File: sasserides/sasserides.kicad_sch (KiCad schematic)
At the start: 129 parts, among them J1 Conn_02x16_Odd_Even, Q1 2N7002

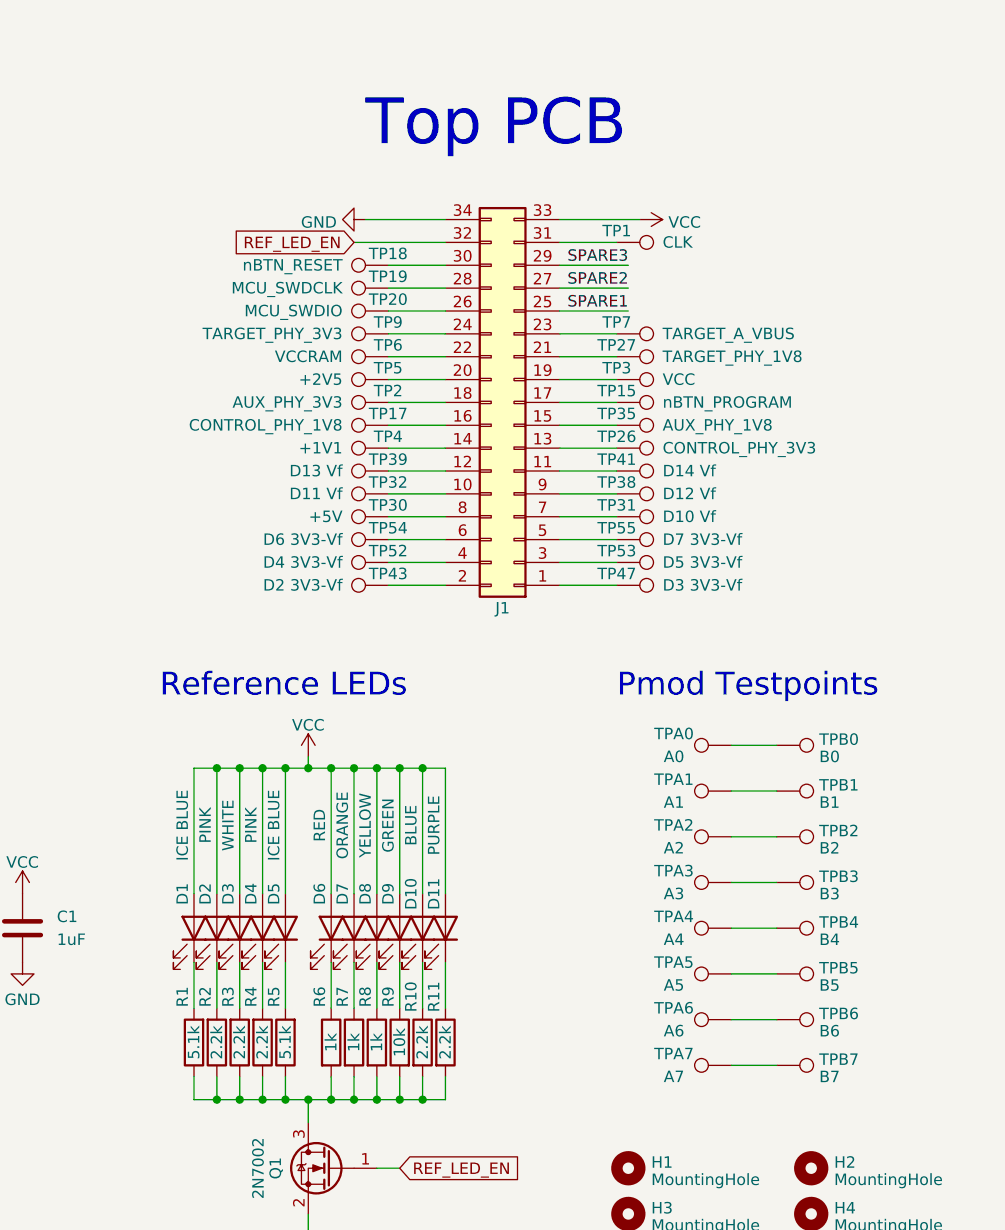
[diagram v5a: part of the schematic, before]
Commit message: Give all nets meaningful names.
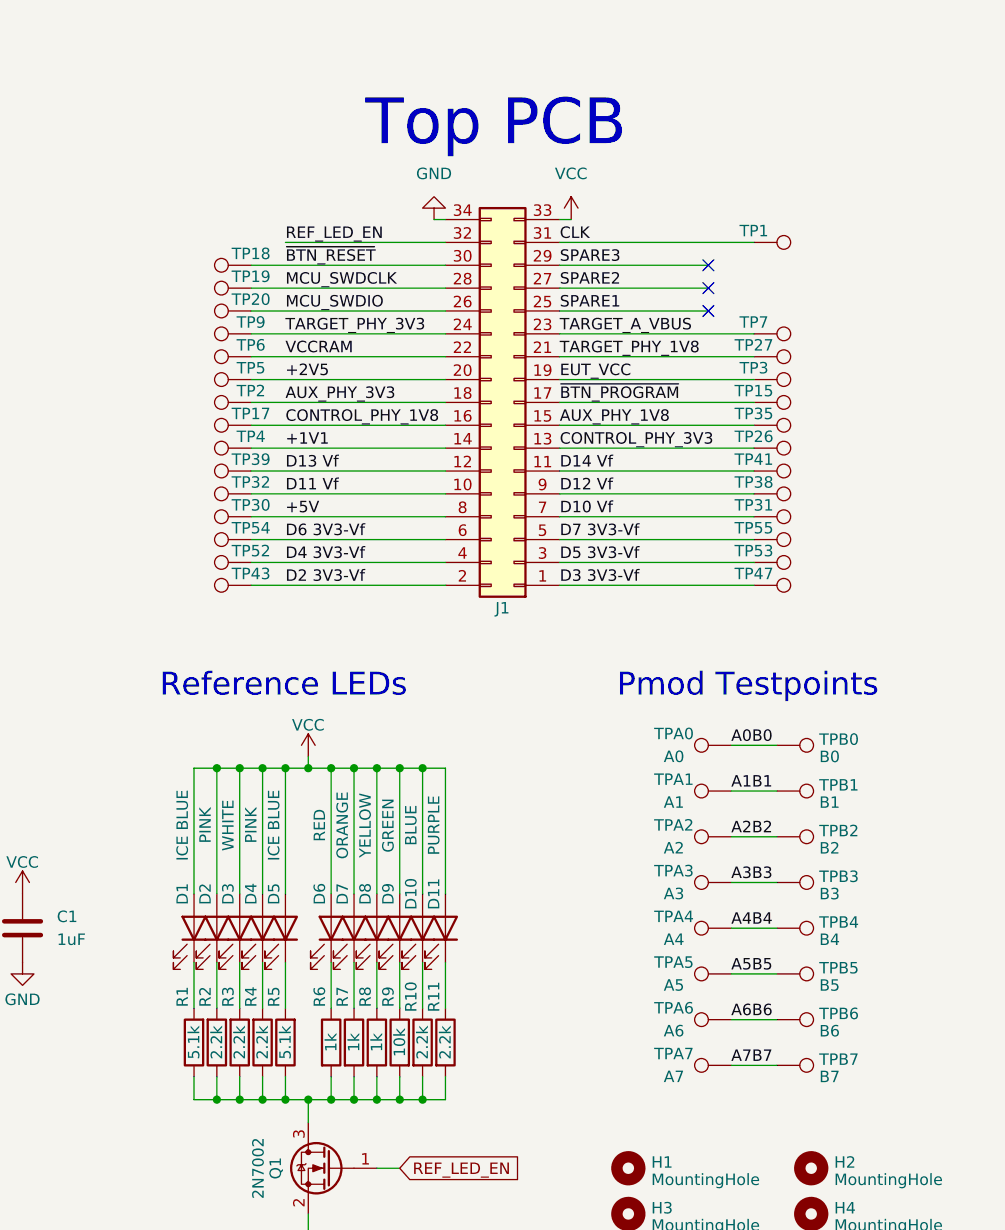
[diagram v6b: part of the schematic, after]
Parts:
- TP1: value CLK -> ~
- TP15: value nBTN_PROGRAM -> ~
- TP17: value CONTROL_PHY_1V8 -> ~
- TP18: value nBTN_RESET -> ~
- TP19: value MCU_SWDCLK -> ~
- TP2: value AUX_PHY_3V3 -> ~
- TP20: value MCU_SWDIO -> ~
- TP26: value CONTROL_PHY_3V3 -> ~
- TP27: value TARGET_PHY_1V8 -> ~
- TP3: value VCC -> ~
- TP30: value +5V -> ~
- TP31: value D10 Vf -> ~
- TP32: value D11 Vf -> ~
- TP35: value AUX_PHY_1V8 -> ~
- TP38: value D12 Vf -> ~
- TP39: value D13 Vf -> ~
- TP4: value +1V1 -> ~
- TP41: value D14 Vf -> ~
- TP43: value D2 3V3-Vf -> ~
- TP47: value D3 3V3-Vf -> ~
- TP5: value +2V5 -> ~
- TP52: value D4 3V3-Vf -> ~
- TP53: value D5 3V3-Vf -> ~
- TP54: value D6 3V3-Vf -> ~
- TP55: value D7 3V3-Vf -> ~
- TP6: value VCCRAM -> ~
- TP7: value TARGET_A_VBUS -> ~
- TP9: value TARGET_PHY_3V3 -> ~
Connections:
- net D3 3V3-Vf: now reaches J1.1 (Pin_1), TP47.1
- net A0B0: now reaches TPA0.1, TPB0.1
- net D11 Vf: now reaches J1.10 (Pin_10), TP32.1
- net D14 Vf: now reaches J1.11 (Pin_11), TP41.1
- net D13 Vf: now reaches J1.12 (Pin_12), TP39.1
- net CONTROL_PHY_3V3: now reaches J1.13 (Pin_13), TP26.1
- net +1V1: now reaches J1.14 (Pin_14), TP4.1
- net AUX_PHY_1V8: now reaches J1.15 (Pin_15), TP35.1
- net CONTROL_PHY_1V8: now reaches J1.16 (Pin_16), TP17.1
- net ~{BTN_PROGRAM}: now reaches J1.17 (Pin_17), TP15.1
- net AUX_PHY_3V3: now reaches J1.18 (Pin_18), TP2.1
- net EUT_VCC: now reaches J1.19 (Pin_19), TP3.1
- net D2 3V3-Vf: now reaches J1.2 (Pin_2), TP43.1
- net +2V5: now reaches J1.20 (Pin_20), TP5.1
- net TARGET_PHY_1V8: now reaches J1.21 (Pin_21), TP27.1
- net VCCRAM: now reaches J1.22 (Pin_22), TP6.1
- net TARGET_A_VBUS: now reaches J1.23 (Pin_23), TP7.1
- net TARGET_PHY_3V3: now reaches J1.24 (Pin_24), TP9.1
- net MCU_SWDIO: now reaches J1.26 (Pin_26), TP20.1
- net MCU_SWDCLK: now reaches J1.28 (Pin_28), TP19.1
- net D5 3V3-Vf: now reaches J1.3 (Pin_3), TP53.1
- net ~{BTN_RESET}: now reaches J1.30 (Pin_30), TP18.1
- net CLK: now reaches J1.31 (Pin_31), TP1.1
- net D4 3V3-Vf: now reaches J1.4 (Pin_4), TP52.1
- net D7 3V3-Vf: now reaches J1.5 (Pin_5), TP55.1
- net D6 3V3-Vf: now reaches J1.6 (Pin_6), TP54.1
- net D10 Vf: now reaches J1.7 (Pin_7), TP31.1
- net +5V: now reaches J1.8 (Pin_8), TP30.1
- net D12 Vf: now reaches J1.9 (Pin_9), TP38.1
- net A3B3: now reaches TPA3.1, TPB3.1
- net A2B2: now reaches TPA2.1, TPB2.1
- net A1B1: now reaches TPA1.1, TPB1.1
- net A5B5: now reaches TPA5.1, TPB5.1
- net A6B6: now reaches TPA6.1, TPB6.1
- net A4B4: now reaches TPA4.1, TPB4.1
- net A7B7: now reaches TPA7.1, TPB7.1
- no-connect marks 44 -> 47
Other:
- moved on the sheet: TP1, TP15, TP17, TP18, TP19, TP2, TP20, TP26, TP27, TP3, TP30, TP31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

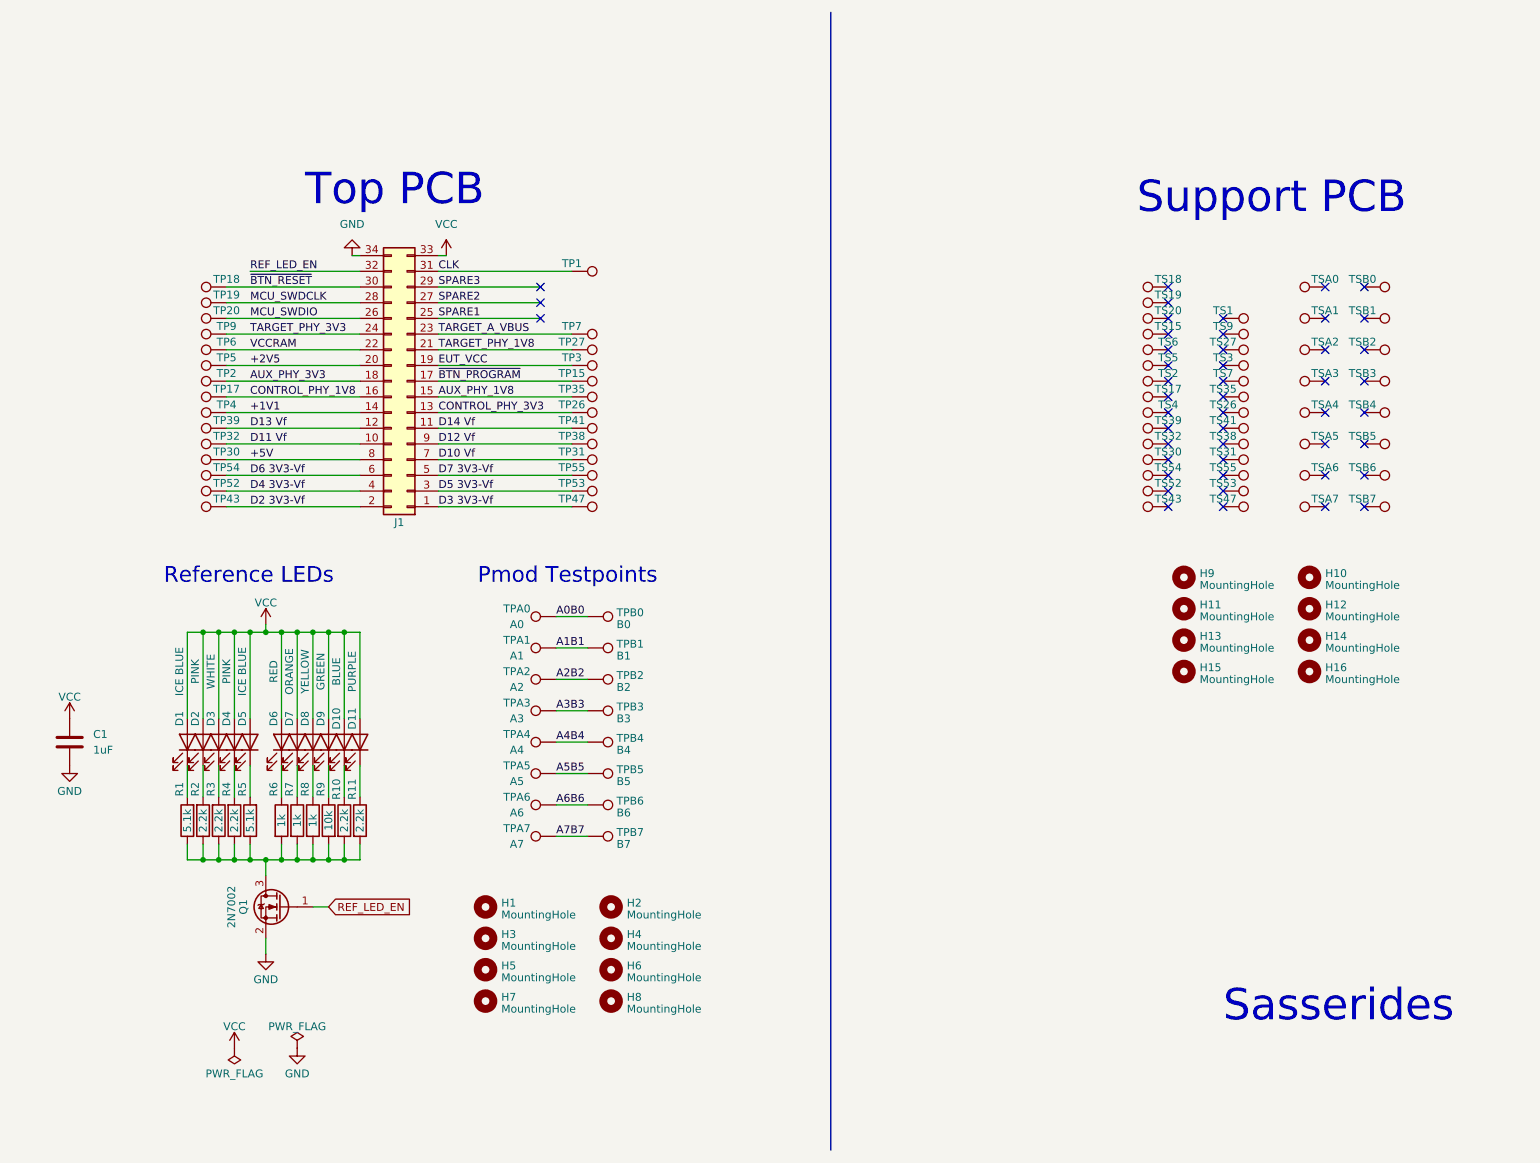
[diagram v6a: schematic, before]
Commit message: Add clock buffer and revise layout.
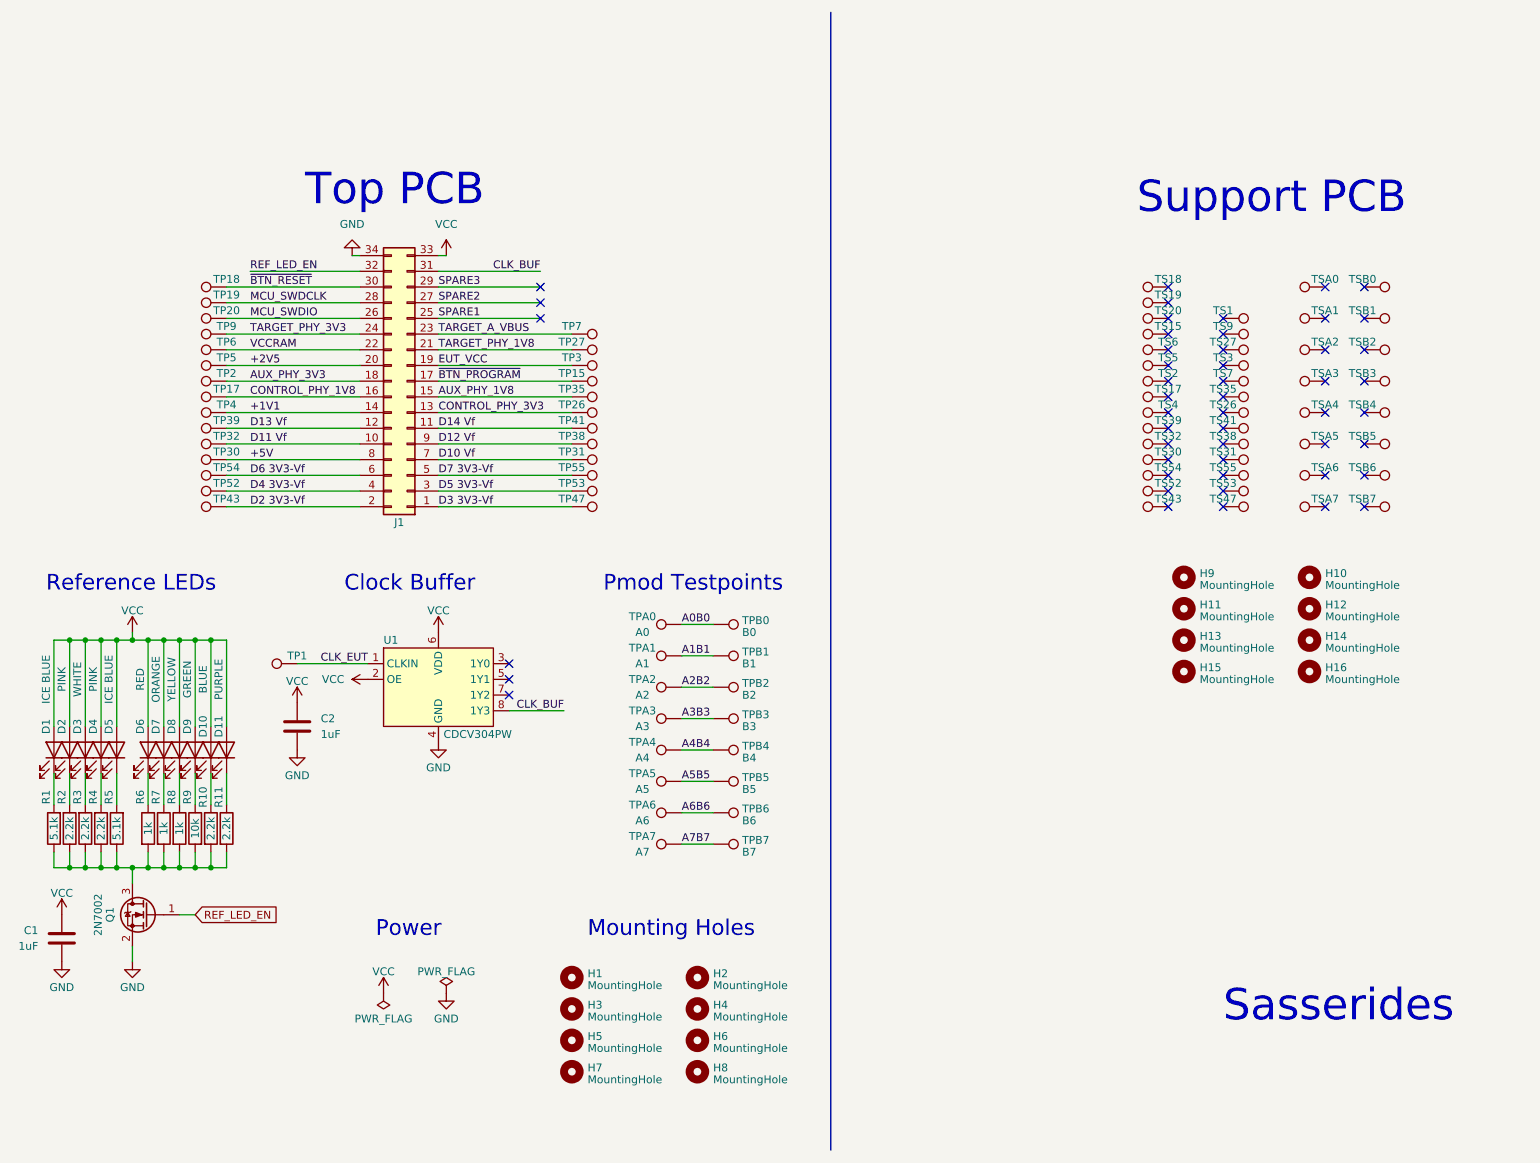
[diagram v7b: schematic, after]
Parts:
- added C2: 1uF, Capacitor_SMD:C_0805_2012Metric, symbol Device:C
- added U1: CDCV304PW, Package_SO:TSSOP-8_4.4x3mm_P0.65mm, symbol tycho:CDCV304PW
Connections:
- net GND: now also C2.2, U1.4 (GND)
- net VCC: now also C2.1, U1.2 (OE), U1.6 (VDD)
- net CLK renamed CLK_BUF
- net CLK_BUF: now also U1.8 (1Y3); no longer TP1.1
- new net CLK_EUT: TP1.1, U1.1 (CLKIN)
- no-connect marks 47 -> 50
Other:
- note added: "Clock Buffer"
- note added: "Mounting Holes"
- note added: "Power"
- moved on the sheet: C1, D1, D10, D11, D2, D3, D4, D5, D6, D7, D8, D9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

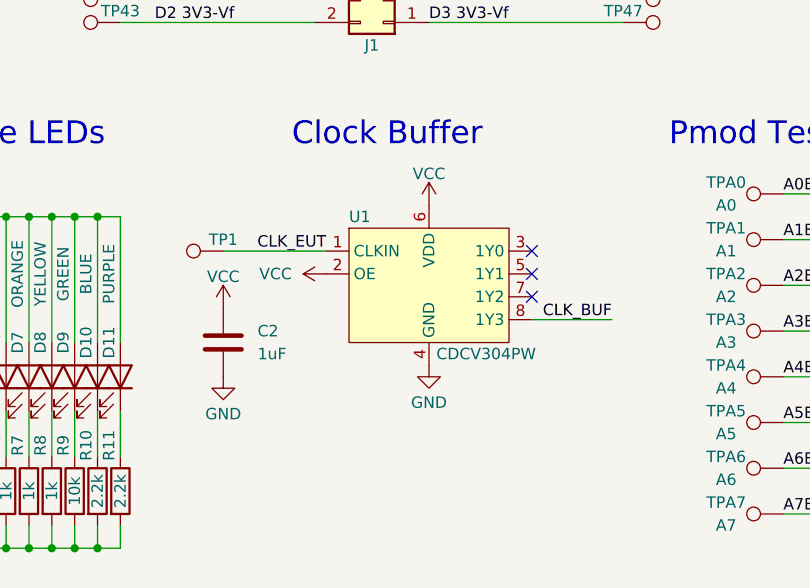
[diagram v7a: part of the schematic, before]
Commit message: Add zero-ohm series resistor at clock driver.
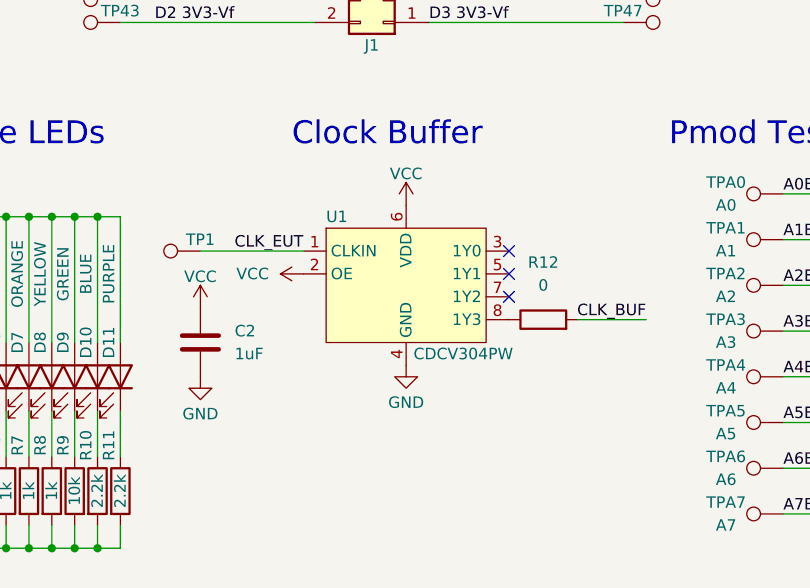
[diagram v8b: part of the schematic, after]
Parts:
- added R12: 0, Resistor_SMD:R_0402_1005Metric, symbol Device:R
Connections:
- net CLK_BUF: now also R12.2; no longer U1.8 (1Y3)
- new net: R12.1, U1.8 (1Y3)
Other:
- moved on the sheet: C2, TP1, U1
